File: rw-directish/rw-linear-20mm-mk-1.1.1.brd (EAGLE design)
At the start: 17.2 x 17.2 mm, 21 parts, among them U1 Tiny25, U10 AMC7135, U11 AMC7135, U12 AMC7135, U2 AMC7135, U3 AMC7135, U4 AMC7135, U5 AMC7135, U6 AMC7135, U7 AMC7135, U8 AMC7135, U9 AMC7135

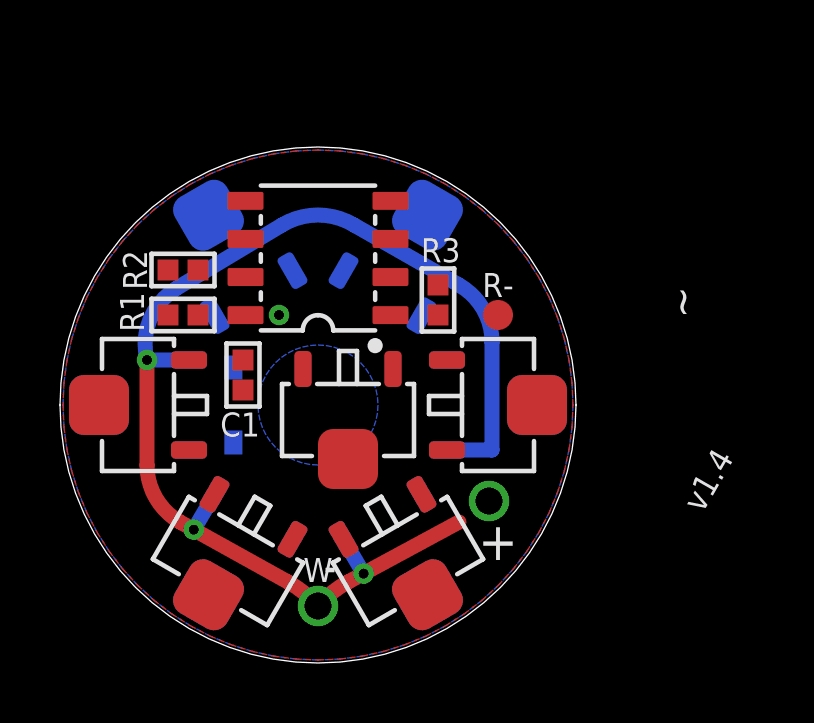
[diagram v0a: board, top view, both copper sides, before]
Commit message: 20mm dual channel linear driver
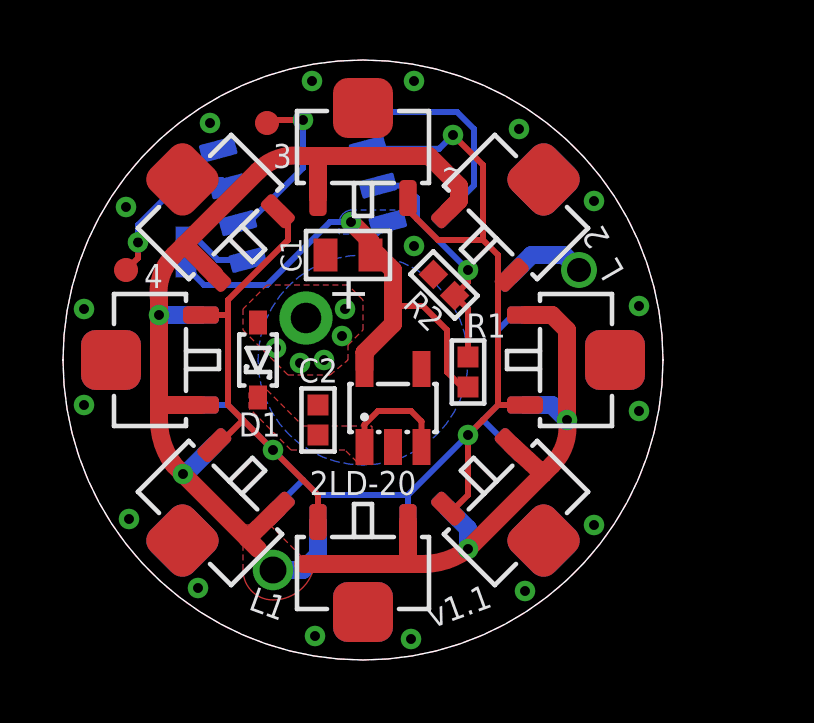
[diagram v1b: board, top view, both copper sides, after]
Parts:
- removed R-: M01SMD-1MM-DIA-NS, a_parts:1X01-SMD-1MM-DIA-NS
- removed W: M011X01-0.9MM-CIR, a_parts:1X01-0.9MM-CIR
- added 3, 4: M01SMD-0.8MM-DIA-NS, a_parts:1X01-SMD-0.8MM-DIA-NS
- added C2: 1u, a_parts:C0402
- added L_1: M011X01-0.9MM-CIR, a_parts:1X01-0.9MM-CIR
- added L_2: M01PTH-0.8MM-CIR, a_parts:1X01-0.8MM-CIR
- added U13, U14, U15: AMC7135, a_parts:SOT89-NOTHERM-ROUNDED-LESS
- added U16: V_REG_SOT-23-5AP2112, a_parts:SOT23-5
- +: value M011X01-0.9MM-CIR -> M01PTH-1MM-CIR-NS; device a_parts:1X01-0.9MM-CIR -> a_parts:1X01-1MM-CIR-NS
- C1: value 1u -> 4u7; device a_parts:C0402 -> a_parts:C0603-TIGHTER
- moved U2 14.2 mm to (15.1, 15.1), flipped to the bottom, turned to 45 degrees
- moved U7 13.9 mm to (10.0, 17.1), flipped to the top, turned to 0 degrees
- moved U6 13.4 mm to (17.1, 10.0), flipped to the top, turned to 270 degrees
- moved U5 13.1 mm to (15.1, 4.90), flipped to the top, turned to 225 degrees
- moved U4 11.7 mm to (10.0, 2.90), flipped to the top, turned to 180 degrees
- moved U3 11.0 mm to (4.90, 4.90), flipped to the top, turned to 135 degrees
- moved U12 10.3 mm to (4.90, 4.90), flipped to the bottom, turned to 225 degrees
- moved R1 9.69 mm to (13.5, 9.60), turned to 270 degrees
- moved R2 8.71 mm to (12.7, 12.5), turned to 315 degrees
- moved + 8.63 mm to (8.10, 11.4)
- moved R3 8.55 mm to (4.10, 13.6), flipped to the bottom
- moved U9 7.86 mm to (17.1, 10.0), flipped to the bottom, turned to 90 degrees
- moved U8 6.63 mm to (15.1, 15.1), flipped to the top, turned to 315 degrees
- moved C1 5.32 mm to (9.50, 13.5), turned to 180 degrees
- moved U11 4.52 mm to (10.0, 2.90), flipped to the bottom, turned to 180 degrees
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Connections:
- removed net PWM_R: U1.5, U12.3
- removed net PWM_W: U1.6, U10.3, U11.3, U2.3, U3.3, U4.3, U5.3, U6.3, U7.3, U8.3, U9.3
- removed net RED_K: R-.P$1, U12.1
- removed net WHITE_K: U10.1, U11.1, U2.1, U3.1, U4.1, U5.1, U6.1, U7.1, U8.1, U9.1, W.P$1
- new net LED1_K: L_1.P$1, U10.1, U11.1, U12.1, U13.1, U14.1, U15.1, U3.1, U4.1, U5.1, U6.1, U7.1, U8.1, U9.1
- new net LED2_K: L_2.1, U2.1
- new net PWM_1: U1.6, U10.3, U11.3, U12.3, U13.3, U14.3, U15.3, U3.3, U4.3, U5.3, U6.3, U7.3, U8.3, U9.3
- new net PWM_2: U1.5, U2.3
- new net VBAT_DC: C2.1, D1.C, U16.1, U16.3
- net 3: now also 3.P$1
- net 4: now also 4.P$1
- net GND: now also C2.2, U13.4, U14.4, U15.4, U16.2, U16.4
- net VBAT: now also +.1; no longer +.P$1
- net VCC: now also U16.5; no longer D1.C
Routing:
- net LED1_K: track 0.00 -> 56.4 mm, vias 0 -> 4
- net PWM_1: track 0.00 -> 56.1 mm, vias 0 -> 3
- net WHITE_K: track 41.1 -> 0.00 mm, vias 3 -> 0
- net VCC: track 0.00 -> 18.2 mm
- net BATT_DIV: track 0.00 -> 7.85 mm, vias 0 -> 1
- net PWM_2: track 0.00 -> 7.19 mm
- net 3: track 0.00 -> 5.82 mm, vias 0 -> 1
- net 4: track 0.00 -> 5.38 mm, vias 0 -> 1
- net VBAT_DC: track 0.00 -> 3.83 mm
- net LED2_K: track 0.00 -> 2.72 mm
- net N$1: track 0.00 -> 2.38 mm
- added copper zone on layer 1, net LED1_K
- added copper zone on layer 1, net VBAT
- added copper zone on layer 1, net VBAT_DC
- added copper zone on layer 16, net VCC
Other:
- board size 17.2 x 17.2 mm -> 20 x 20 mm
- board text added: "2"
- board text added: "2LD-20"
- board text added: "2xLD-20"
- board text added: "L"
- board text added: "L1"
- board text added: "PWM"
